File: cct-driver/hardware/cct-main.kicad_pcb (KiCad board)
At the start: 2 copper layers, 130 x 164 mm, 217 parts, among them J1 C707824, J10 C37815, J11 C474923, J2 C165948, J3 C441333, J4 C441333, J5 C441333, J6 C441333, J7 C441333, J8 C441333, J9 C2906270, Q1 C3281500, Q10 C2890395, Q11 C2890395, Q12 C2890395, Q13 C2890395, Q14 C2890395, Q15 C2890395, Q16 C2890395, Q17 C2890395, Q18 C2890395, Q2 C3281500, Q3 C20526, Q4 C2146, Q5 C2146, Q6 C20526, Q7 C2890395, Q8 C2890395, Q9 C2890395, SW1 C318884, SW2 C318884, U1 C2864837, U2 C524806, U3 C6186, U4 C701341, U5 C84681, U6 C52140501, U7 C52140501

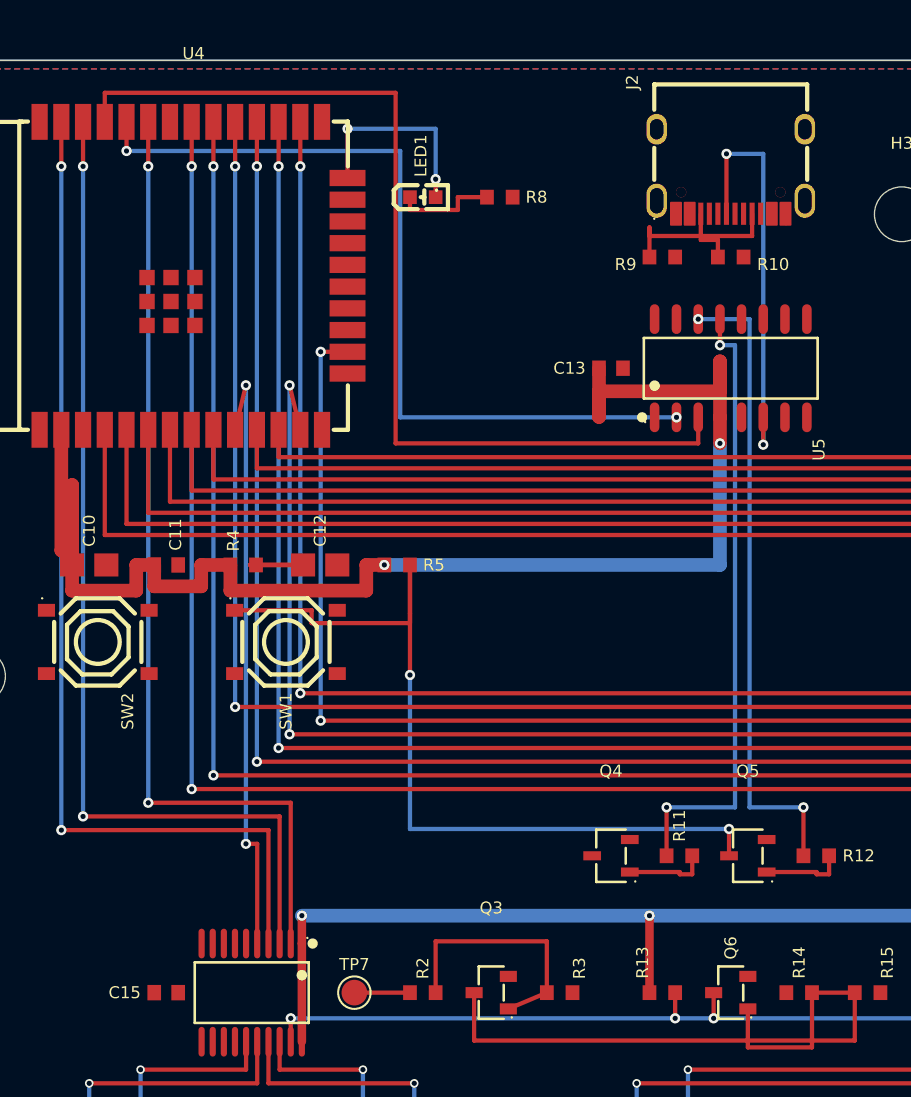
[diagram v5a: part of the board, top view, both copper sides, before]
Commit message: v2 布线:布不通的现在会说清「是谁挡的」;未连接 47 → 48,短路仍是 0
**最有用的一处改动:布不通不再只报一句「布不通」,而是报出挡路的是谁。**
`_clean()` 每次判定失败都记下挡路的那一位,失败时按出现次数报前三名,例如:

    ✗ EN     C12 → SW2   挡路的:走线[V3P3]×17836、焊盘[V3P3]×4054、焊盘[GND]×3300

有了这个,剩下的活就不是「再试试别的拐法」,而是能指名道姓地做取舍。

另外两条通了:
- **OE_CTRL(失效安全链的输入)** —— 它要从 U4 右侧脚绕到驱动区,原来被 LED1/R8
  挡在 x≈30 那条唯一的竖道上;把这两件挪到 (32,15)/(36,15) 就通了
- **IO0** —— 它和 12 路 PWM 一样在 U4 的**上排**,处境完全相同,
  所以并进同一套「底层竖道」分配里,不再单独找缝

    走线 793 段 · 过孔 260 颗 · 覆铜 16 块
    **短路 0 · 走线交叉 0**
    未连接 48 条;明确报出布不通的 11 条,每条都带挡路者
    网表与原理图 525 条零差异

**剩下这 11 条挤在同一块地方(U4 周边的 A1/A2),而且互相挤** —— 给这条腾出路,
另一条就被顶掉(这一版就换掉了两条)。这不是布线技巧问题,是那一块**摆位太密**,
要么给 A1/A2 加地方、要么重排,属于设计取舍,留给下一轮先定方向再动手。

Co-Authored-By: Claude <noreply@anthropic.com>
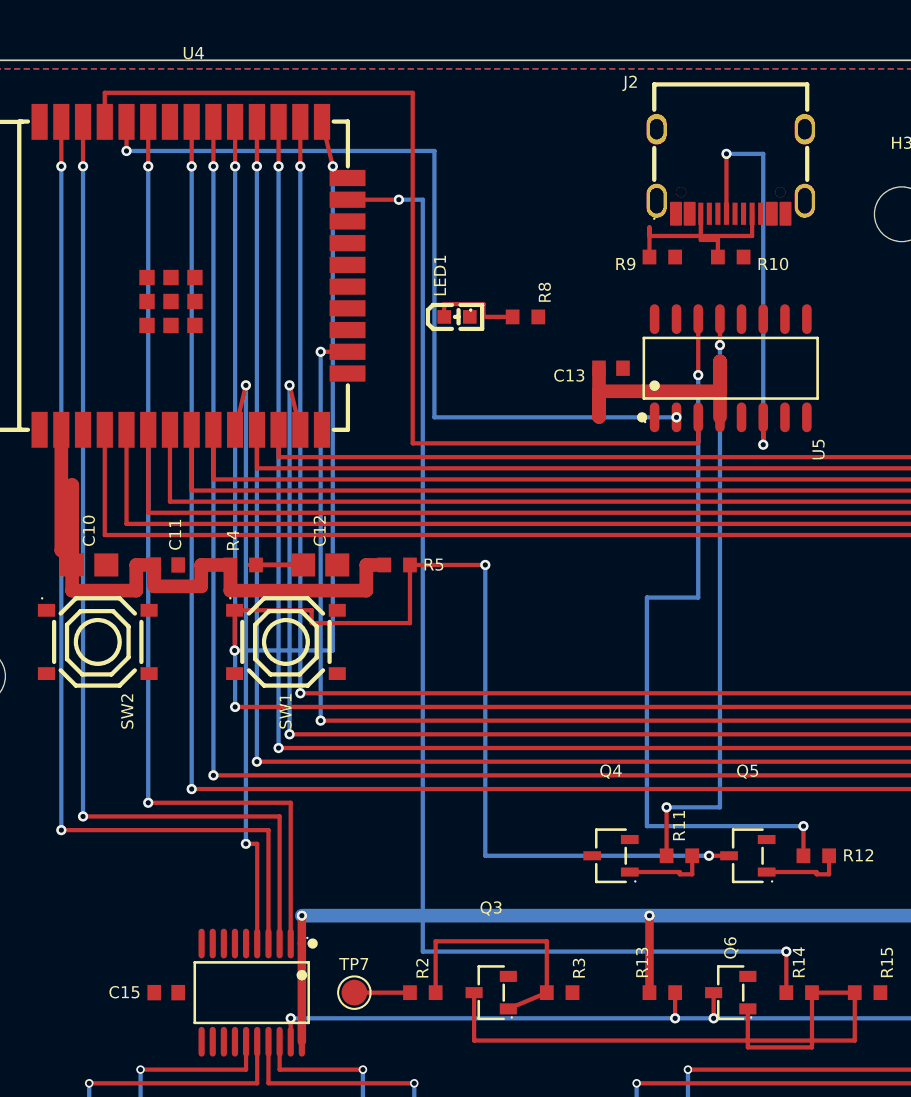
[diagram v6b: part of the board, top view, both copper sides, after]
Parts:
- moved LED1 7.28 mm to (32.0, 15.0)
- moved R8 7.16 mm to (36.0, 15.0)
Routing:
- net V5_SYS: track 263.6 -> 183.0 mm
- net V24_LOGIC: track 164.2 -> 244.8 mm
- net OE_CTRL: track 0.00 -> 72.0 mm, vias 0 -> 2
- net IO0: track 50.0 -> 89.1 mm, vias 2 -> 4
- net V3P3: track 209.9 -> 181.6 mm, vias 4 -> 2
- net LED_STATUS: track 12.0 -> 0.00 mm, vias 2 -> 0
- net RTS: track 37.5 -> 43.5 mm
- net DTR: track 36.2 -> 34.5 mm
- net LED1_K: track 6.00 -> 5.50 mm

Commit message: v2 丝印功能标注:通道号 / 引脚名 / 极性 / 接口电压 / 板名 / 「先关电源再插拔 J1」
老的 `gen_silk.py` 坐标是 110×145 那块板的,整份对不上,另起一份 `gen_silk_v2.py`。
它**只写板级丝印文字,一个铜箔、一个位号都不碰**;位号归位仍归 `gen_silk_refdes_fix.py`。

写了 58 条:六路端子的 `CHn` + `V+ CW WW`、指示灯的 CW/WW、进线的 `24V IN` 与 `+ -`、
`F1 ATO 15A`、`F2-F7 4A T 32V`、四个接口的电压标注、九个测试焊盘的网络名、板名版本。

**人类 8/15 确认的操作规矩上板了**:
`24V MAX 12A - POWER OFF BEFORE UNPLUG J1` 写在 **J1 正下方的支撑带**里(那一片是空板,
插拔时眼睛正好看得到),下板边另有一句 `POWER OFF BEFORE UNPLUG` 给六路灯带端子。

**流水线顺序改了**:丝印要排在位号归位**之前**,好让位号躲开这些功能标注 ——
反过来跑,丝印重叠从 24 条涨到 47 条。新顺序:
    gen_pcb_v2.py → gen_silk_v2.py → gen_silk_refdes_fix.py → gen_route_v2.py

文字位置是**对着渲染图逐条改出来的**,不是拍脑袋:第一版有三处栽了 ——
警示句伸出板框外、`4A T` 和位号 `F7` 糊成「4A7T」、端子的 `V+ CW WW` 被插座本体挡住看不见。
现在端子那两行落在 MOS 下沿与端子体上沿之间那 3.36mm 里,保险丝规格改成在脊椎带写一行总的。

Co-Authored-By: Claude <noreply@anthropic.com>
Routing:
- net IO0: track 89.1 -> 50.0 mm, vias 4 -> 2
- net CC2: track 3.53 -> 0.00 mm
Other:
- board text added: "+"
- board text added: "-"
- board text added: "24V IN"
- board text added: "24V MAX 12A - POWER OFF BEFORE UNPLUG J1"
- board text added: "3V3"
- board text added: "5V"
- board text added: "6CH CCT LED DRIVER 24V 12A"
- board text added: "CH1"
- board text added: "CH2"
- board text added: "CH3"
- board text added: "CH4"
- board text added: "CH5"
- board text added: "CH6"
- board text added: "CW"
- board text added: "D1W"
- board text added: "F1 ATO 15A"
- board text added: "F2-F7 4A T 32V"
- board text added: "G1W"
- board text added: "GND"
- board text added: "I2C 3.3V"
- board text added: "OFF"
- board text added: "PG"
- board text added: "POWER OFF BEFORE UNPLUG"
- board text added: "SW1-4 + GND"
- board text added: "UART 5V"
- board text added: "USB-C PROG"
- board text added: "V+"
- board text added: "V24"
- board text added: "WW"
- board text added: "cct-driver v2"
